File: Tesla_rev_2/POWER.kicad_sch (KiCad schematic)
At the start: 20 parts, among them J11 Screw_Terminal_01x03, U8 AP63203WU

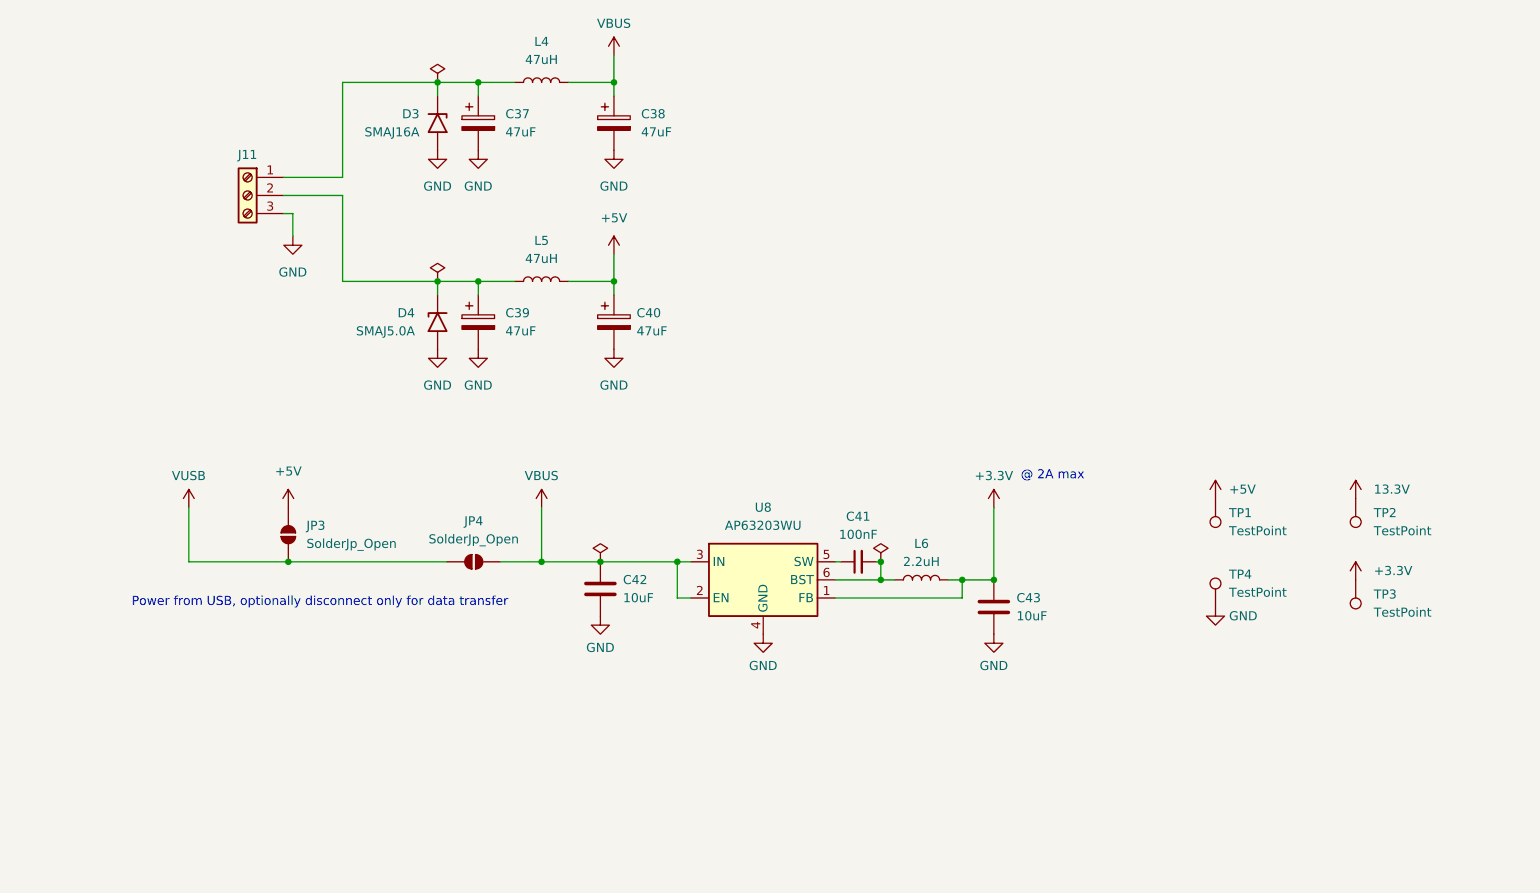
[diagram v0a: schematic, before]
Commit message: Netclasses, part Nums, LPF adjust
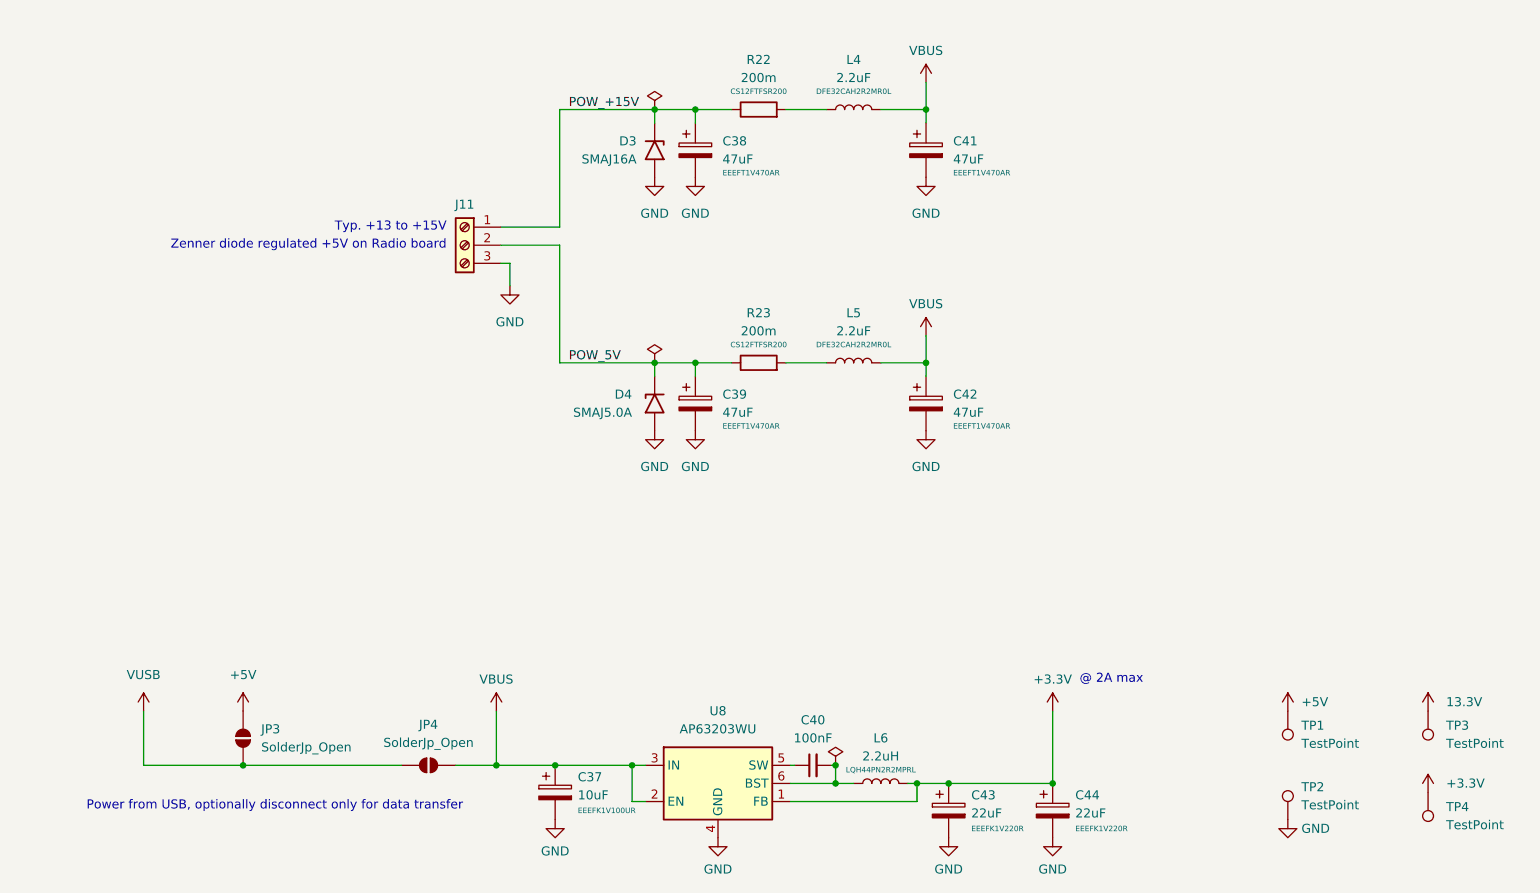
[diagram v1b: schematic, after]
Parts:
- removed C40: 47uF, symbol Device:C_Polarized
- removed C42, C43: 10uF, symbol Device:C
- added C41, C42: 47uF, symbol Device:C_Polarized
- added C43, C44: 22uF, symbol Device:C_Polarized
- added R22, R23: 200m, Resistor_SMD:R_2512_6332Metric, symbol Device:R
- C37: value 47uF -> 10uF; Part_num (none) -> EEEFK1V100UR
- C38, C39: Part_num (none) -> EEEFT1V470AR
- L4, L5: value 47uH -> 2.2uF; Part_num (none) -> DFE32CAH2R2MR0L
- L6: Part_num (none) -> LQH44PN2R2MPRL
- renumbered C41 to C40, TP4 to TP2, TP2 to TP3, TP3 to TP4
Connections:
- net +3.3V: now also C43.1, C44.1
- net +5V: no longer L5.2
- net GND: now also C41.2, C42.2, C43.2, C44.2
- net VBUS: now also C37.1, L5.2, C41.1, C42.1; no longer C38.1
- net POW_5V: now reaches C39.1, D4.1 (A1), J11.2 (Pin_2)
- net POW_5V: now also R23.1; no longer L5.1
- net POW_+15V: now reaches D3.1 (A1), J11.1 (Pin_1)
- net POW_+15V: now also C38.1, R22.1; no longer C37.1, L4.1
- new net: L4.1, R22.2
- new net: L5.1, R23.2
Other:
- note added: "Typ. +13 to +15V"
- note added: "Zenner diode regulated +5V on Radio board"
- title: (none) -> Tesla sextant BT
- moved on the sheet: C40, D3, D4, J11, JP3, JP4, L4, L6, TP1, TP2, TP3, TP4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
